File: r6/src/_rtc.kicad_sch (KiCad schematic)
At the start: 9 parts, among them U13 DS3231MZ, U14 74LVC1G07DCK

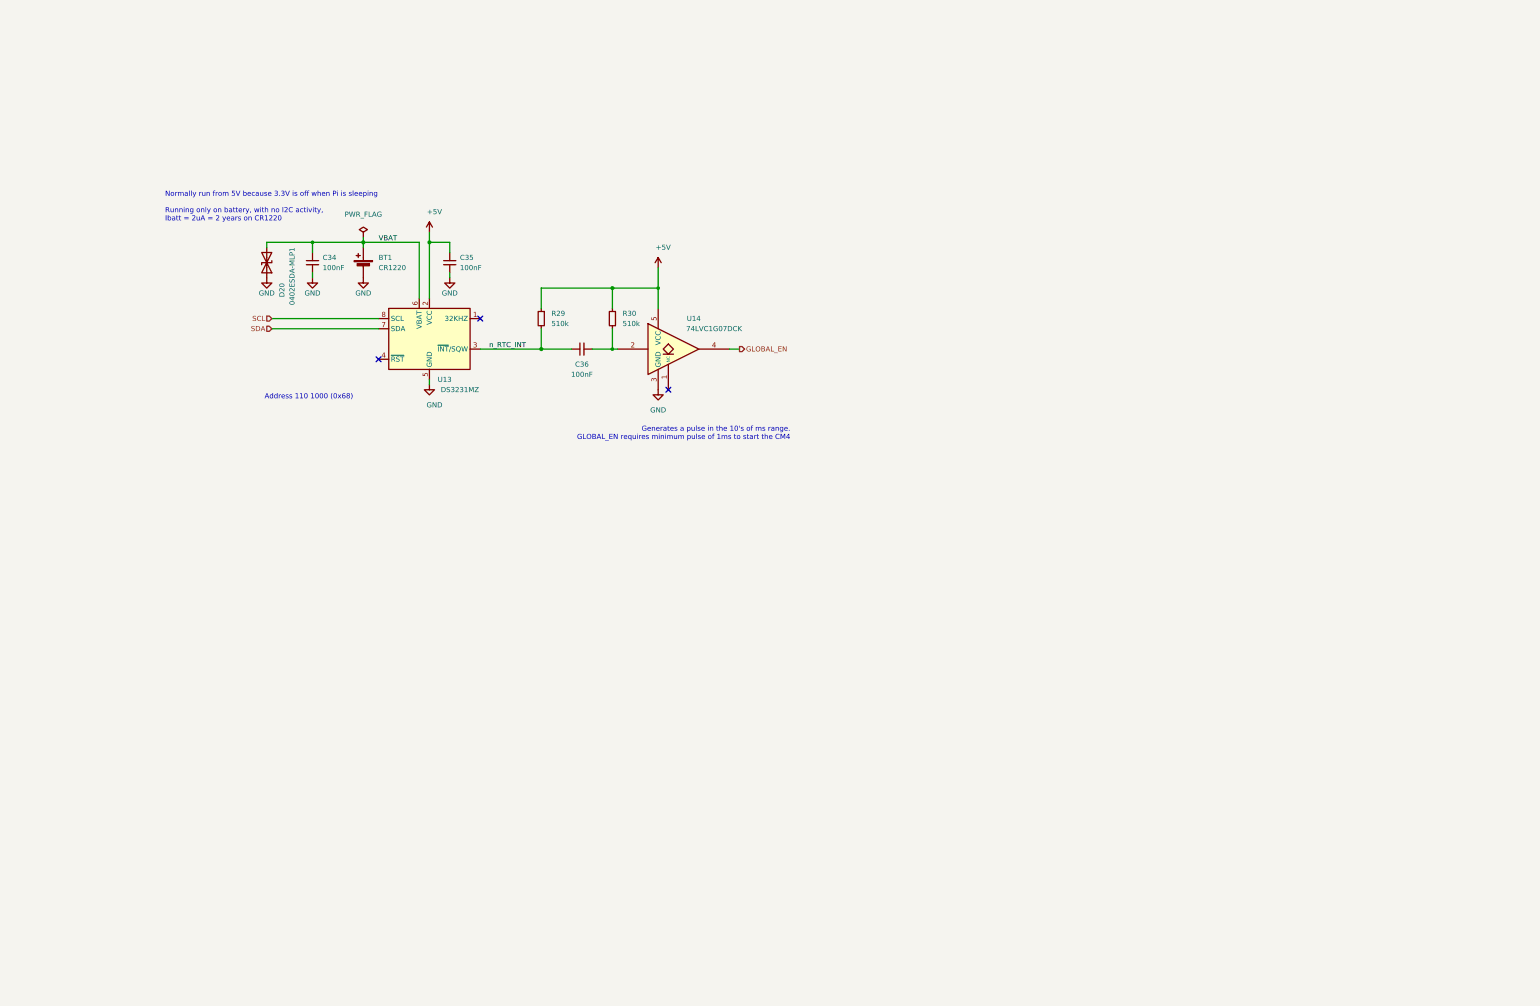
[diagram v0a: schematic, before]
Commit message: r6: experimental revision of the r5 main board (unbuilt)
Filtered plug-in mic bias (R104 100R, Q25 supplied ahead of it),
4.7 nF ADC input filter, RV-3032 RTC on a new 3.3 V always-on rail,
Schmitt wake buffer, ADS1115 four-rail voltage monitoring, and a latched
modem SAFE_PWR_REMOVE/VGPIO shutdown confirmation (r5 erratum 5).

Outline, stack, all 37 fixed interfaces, USB and mic-input copper and
all r5 test points are unchanged. Designed and routed with AI coding
agents, reviewed by the author. No board has been built or measured.
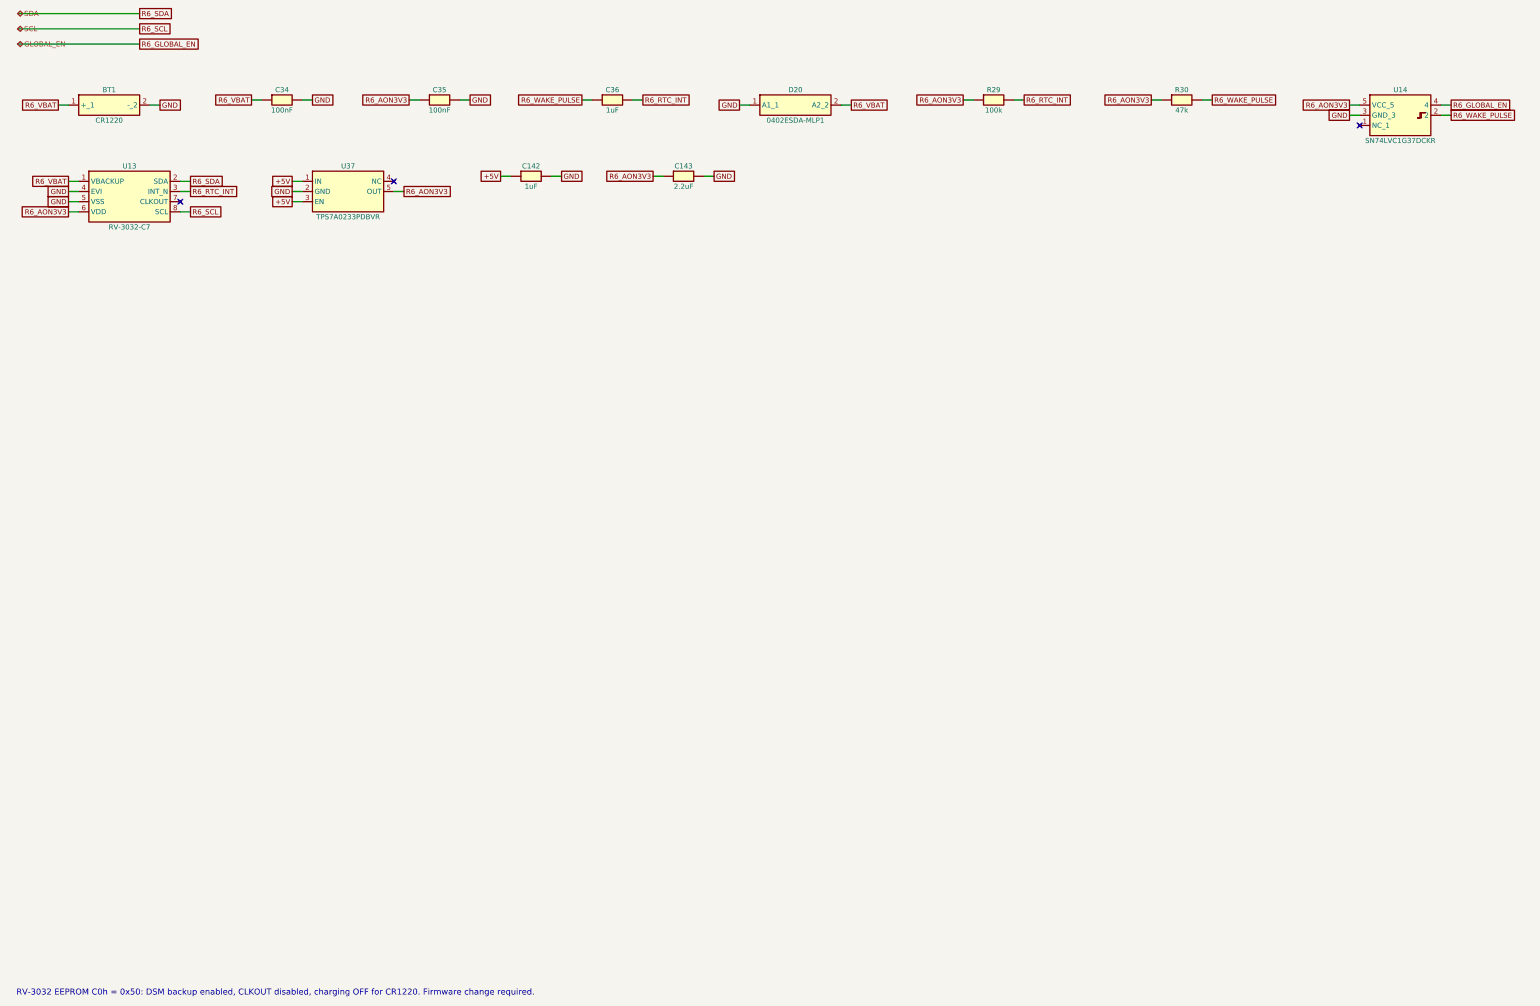
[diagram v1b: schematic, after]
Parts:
- removed BT1: CR1220, jeffmakes-footprints:Keystone-3000-CR1220-CR1216, symbol Device:Battery_Cell
- removed C34, C35, C36: 100nF, Capacitor_SMD:C_0402_1005Metric, symbol Device:C_Small
- removed D20: 0402ESDA-MLP1, Diode_SMD:D_0402_1005Metric, symbol Device:D_TVS
- removed R29, R30: 510k, Resistor_SMD:R_0402_1005Metric, symbol Device:R_Small
- removed U13: DS3231MZ, Package_SO:SOIC-8_3.9x4.9mm_P1.27mm, symbol Timer_RTC:DS3231MZ
- removed U14: 74LVC1G07DCK, Package_TO_SOT_SMD:SOT-353_SC-70-5, symbol 74xGxx:74LVC1G07
- added BT1: CR1220, jeffmakes-footprints:Keystone-3000-CR1220-CR1216, symbol bugg_r6:BT1
- added C142: 1uF, Capacitor_SMD:C_0603_1608Metric, symbol bugg_r6:C142
- added C143: 2.2uF, Capacitor_SMD:C_0603_1608Metric, symbol bugg_r6:C143
- added C34: 100nF, Capacitor_SMD:C_0402_1005Metric, symbol bugg_r6:C34
- added C35: 100nF, Capacitor_SMD:C_0402_1005Metric, symbol bugg_r6:C35
- added C36: 1uF, Capacitor_SMD:C_0402_1005Metric, symbol bugg_r6:C36
- added D20: 0402ESDA-MLP1, Diode_SMD:D_0402_1005Metric, symbol bugg_r6:D20
- added R29: 100k, Resistor_SMD:R_0402_1005Metric, symbol bugg_r6:R29
- added R30: 47k, Resistor_SMD:R_0402_1005Metric, symbol bugg_r6:R30
- added U13: RV-3032-C7, Package_SON:MicroCrystal_C7_SON-8_1.5x3.2mm_P0.9mm, symbol bugg_r6:U13
- added U14: SN74LVC1G37DCKR, Package_TO_SOT_SMD:SOT-353_SC-70-5, symbol bugg_r6:U14
- added U37: TPS7A0233PDBVR, Package_TO_SOT_SMD:SOT-23-5, symbol bugg_r6:U37
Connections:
- net +5V: now also C142.1, U37.1 (IN), U37.3 (EN)
- net GND: now also BT1.2 (-_2), C142.2, C143.2, C34.2, C35.2, D20.1 (A1_1), U13.4 (EVI), U13.5 (VSS), U14.3 (GND_3), U37.2 (GND)
- new net R6_AON3V3: C143.1, C35.1, R29.1, R30.1, U13.6 (VDD), U14.5 (VCC_5), U37.5 (OUT)
- new net R6_GLOBAL_EN: U14.4
- new net R6_RTC_INT: C36.2, R29.2, U13.3 (INT_N)
- new net R6_SCL: U13.8 (SCL)
- new net R6_SDA: U13.2 (SDA)
- new net R6_VBAT: BT1.1 (+_1), C34.1, D20.2 (A2_2), U13.1 (VBACKUP)
- new net R6_WAKE_PULSE: C36.1, R30.2, U14.2
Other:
- note added: "RV-3032 EEPROM C0h = 0x50: DSM backup enabled, CLKOUT disabled, charging OFF for CR1220. Firmware change required."
- note removed: "Address 110 1000 (0x68)"
- note removed: "Generates a pulse in the 10's of ms range. GLOBAL_EN requires minimum pulse of 1ms to start the CM4"
- note removed: "Normally run from 5V because 3.3V is off when Pi is sleeping Running only on battery, with no I2C activity, Ibatt = 2uA = 2 years on CR1220"
- company: (none) -> Alauda; derived from Bugg r5, CC BY-NC-SA 4.0
- title: (none) -> Bugg r6 experimental derivative - RTC
